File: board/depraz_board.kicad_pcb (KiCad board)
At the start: 2 copper layers, 60 x 40 mm, 15 parts, among them J1 Switches, J2 PIC Programmer, J3 USB, U1 PIC16F1454-IP, U2 TXB0104D, U3 TXB0104D, U4 S-817B20AY-B2-U, U5 PMW3389DM

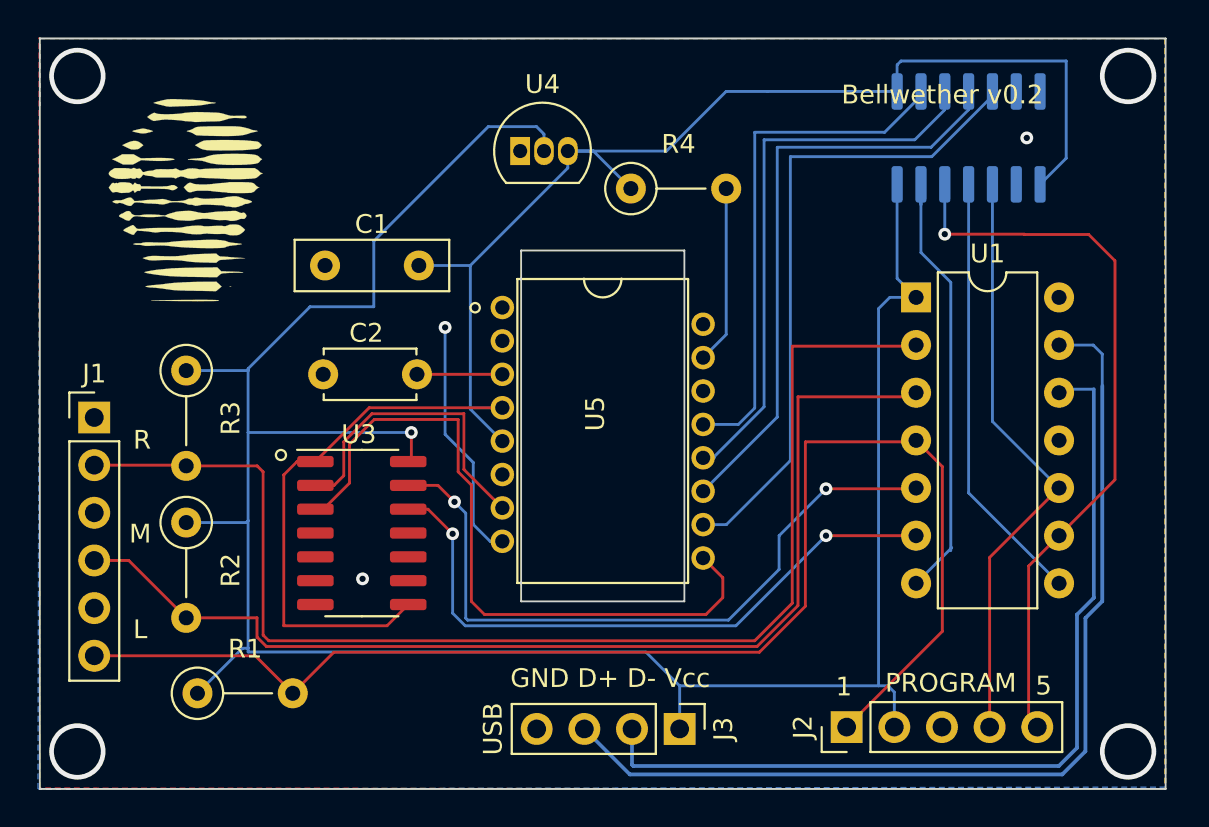
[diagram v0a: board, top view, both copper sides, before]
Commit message: New layout for a STM32 based Depraz replica with quadrature outputs.
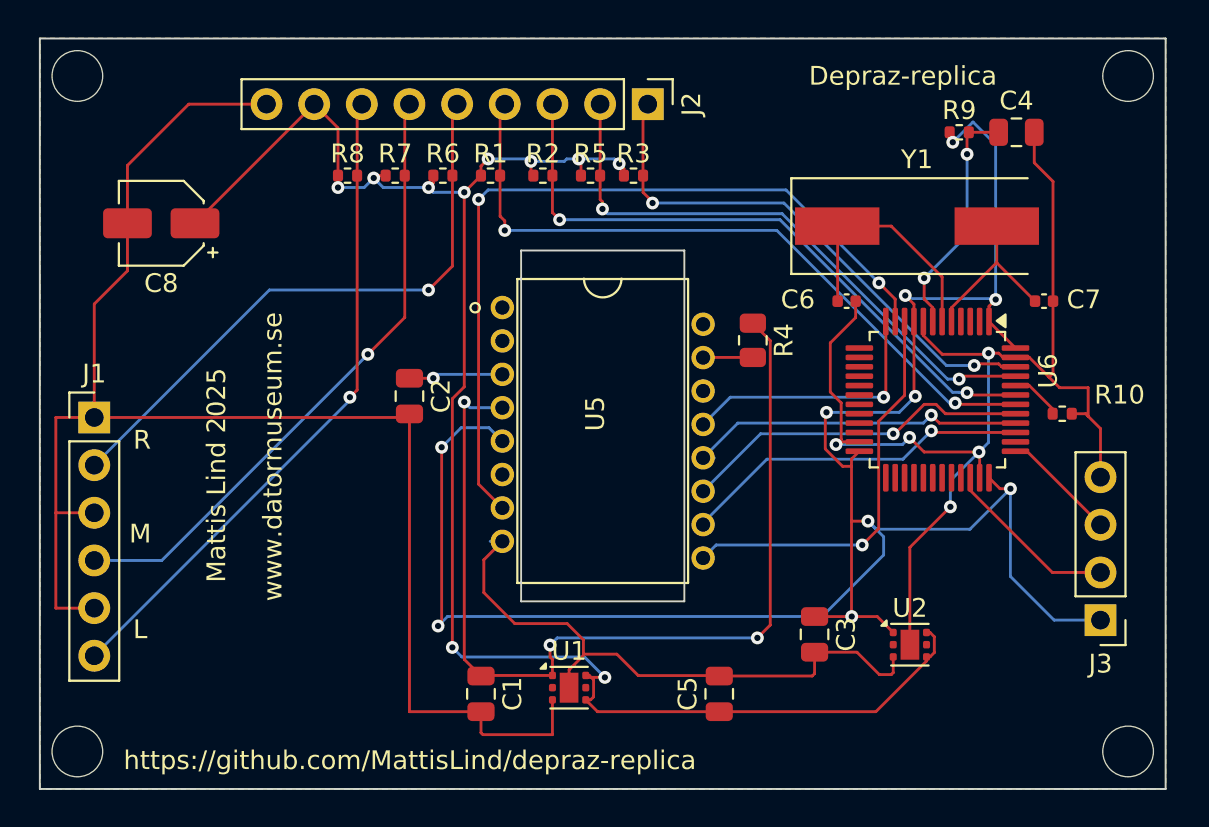
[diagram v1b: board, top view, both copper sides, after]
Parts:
- removed G***: LOGO, depraz_board:pjw
- removed U3: TXB0104D, Package_SO:SOIC-14_3.9x8.7mm_P1.27mm
- removed U4: S-817B20AY-B2-U, Package_TO_SOT_THT:TO-92L_Inline
- added C3: 1u, Capacitor_SMD:C_0805_2012Metric, F.Cu at (161.3, 91.8)
- added C4: 1u, Capacitor_SMD:C_0805_2012Metric, F.Cu at (172.1, 65.0)
- added C5: 1u, Capacitor_SMD:C_0805_2012Metric, F.Cu at (156.2, 94.9)
- added C6: 20p, Capacitor_SMD:C_0402_1005Metric, F.Cu at (163.0, 74.0)
- added C7: 20p, Capacitor_SMD:C_0402_1005Metric, F.Cu at (173.5, 74.0)
- added C8: 22u, Capacitor_SMD:CP_Elec_4x5.4, F.Cu at (126.5, 69.8)
- added H1: MountingHole, MountingHole:MountingHole_2.7mm_M2.5, F.Cu at (122.0, 98.0)
- added H2: MountingHole, MountingHole:MountingHole_2.7mm_M2.5, F.Cu at (122.0, 62.0)
- added H3: MountingHole, MountingHole:MountingHole_2.7mm_M2.5, F.Cu at (178.0, 62.0)
- added H4: MountingHole, MountingHole:MountingHole_2.7mm_M2.5, F.Cu at (178.0, 98.0)
- added R10: 2k, Resistor_SMD:R_0402_1005Metric, F.Cu at (174.5, 80.0)
- added R5: 2k, Resistor_SMD:R_0402_1005Metric, F.Cu at (149.3, 67.3)
- added R6: 2k, Resistor_SMD:R_0402_1005Metric, F.Cu at (141.5, 67.3)
- added R7: 2k, Resistor_SMD:R_0402_1005Metric, F.Cu at (138.9, 67.3)
- added R8: 2k, Resistor_SMD:R_0402_1005Metric, F.Cu at (136.4, 67.3)
- added R9: 2k, Resistor_SMD:R_0402_1005Metric, F.Cu at (169.0, 65.0)
- added U6: STM32F103C8Tx, Package_QFP:LQFP-48_7x7mm_P0.5mm, F.Cu at (167.8, 79.2)
- added Y1: Crystal, Crystal:Crystal_SMD_HC49-SD, F.Cu at (166.8, 70.0)
- C1: value 0.1uF -> 1u; footprint Capacitor_THT:C_Disc_D8.0mm_W2.5mm_P5.00mm -> Capacitor_SMD:C_0805_2012Metric
- C2: footprint Capacitor_THT:C_Disc_D4.7mm_W2.5mm_P5.00mm -> Capacitor_SMD:C_0805_2012Metric
- J2: value PIC Programmer -> Host; footprint Connector_PinHeader_2.54mm:PinHeader_1x05_P2.54mm_Vertical -> Connector_PinHeader_2.54mm:PinHeader_1x09_P2.54mm_Vertical
- J3: value USB -> SWD
- R1, R2, R3: value 1M -> 2k; footprint Resistor_THT:R_Axial_DIN0207_L6.3mm_D2.5mm_P5.08mm_Vertical -> Resistor_SMD:R_0402_1005Metric
- R4: footprint Resistor_THT:R_Axial_DIN0207_L6.3mm_D2.5mm_P5.08mm_Vertical -> Resistor_SMD:R_0805_2012Metric
- U1: value PIC16F1454-IP -> TLV75519PDRV; footprint Package_DIP:DIP-14_W7.62mm -> Package_SON:WSON-6-1EP_2x2mm_P0.65mm_EP1x1.6mm
- U2: value TXB0104D -> TLV75533PDRV; footprint Package_SO:SOIC-14_3.9x8.7mm_P1.27mm -> Package_SON:WSON-6-1EP_2x2mm_P0.65mm_EP1x1.6mm; moved to F.Cu
- moved J2 34.9 mm to (152.4, 63.5), turned to -90 degrees
- moved R1 31.7 mm to (144.0, 67.3)
- moved U1 27.8 mm to (148.2, 94.6)
- moved U2 27.2 mm to (166.4, 92.3), turned to 0 degrees
- moved R2 26.5 mm to (146.8, 67.3), turned to 0 degrees
- moved R3 26.0 mm to (151.6, 67.3), turned to 0 degrees
- moved J3 23.2 mm to (176.5, 91.0), turned to 180 degrees
- moved C1 23.1 mm to (143.5, 94.9), turned to -90 degrees
- moved R4 10.4 mm to (158.0, 76.1), turned to -90 degrees
- moved C2 1.23 mm to (139.7, 79.1), turned to -90 degrees
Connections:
- C1 pad 1: 2V -> 1.9V
- J1 pad 2: Net-(J1-Pad2) -> Net-(J1-Pin_2)
- J1 pad 4: Net-(J1-Pad4) -> Net-(J1-Pin_4)
- J1 pad 6: Net-(J1-Pad6) -> Net-(J1-Pin_6)
- J2 pad 1: Net-(J1-Pad6) -> Net-(J2-Pin_1)
- J2 pad 2: USB_5V -> Net-(J2-Pin_2)
- J2 pad 3: GND -> Net-(J2-Pin_3)
- J2 pad 4: Net-(J2-Pad4) -> Net-(J2-Pin_4)
- J2 pad 5: Net-(J2-Pad5) -> Net-(J1-Pin_2)
- J3 pad 1: USB_5V -> +3.3V
- J3 pad 2: USB_D- -> Net-(J3-Pin_2)
- J3 pad 3: USB_D+ -> Net-(J3-Pin_3)
- R1 pad 1: USB_5V -> +5V
- R1 pad 2: Net-(J1-Pad6) -> Net-(J2-Pin_4)
- R2 pad 1: USB_5V -> +5V
- R2 pad 2: Net-(J1-Pad4) -> Net-(J2-Pin_3)
- R3 pad 1: USB_5V -> +5V
- R3 pad 2: Net-(J1-Pad2) -> Net-(J2-Pin_1)
- R4 pad 1: 2V -> 1.9V
- U1 pad 1: USB_5V -> 1.9V
- U1 pad 2: Net-(J1-Pad2) -> unconnected-(U1-NC-Pad2)
- U1 pad 3: Net-(J1-Pad4) -> GND
- U1 pad 4: Net-(J1-Pad6) -> +5V
- U1 pad 5: Net-(U1-Pad5) -> unconnected-(U1-NC-Pad5)
- U1 pad 6: Net-(U1-Pad6) -> +5V
- U1 pad 7: Net-(U1-Pad7) -> GND
- U2 pad 1: 2V -> +3.3V
- U2 pad 2: Net-(U2-Pad2) -> unconnected-(U2-NC-Pad2)
- U2 pad 3: Net-(U2-Pad3) -> GND
- U2 pad 4: Net-(U2-Pad4) -> +5V
- U2 pad 5: Net-(U2-Pad5) -> unconnected-(U2-NC-Pad5)
- U2 pad 6: Net-(U2-Pad6) -> +5V
- U5 pad 1: Net-(U5-Pad1) -> unconnected-(U5-NC-Pad1)
- U5 pad 10: Net-(U2-Pad5) -> Net-(U5-SCLK)
- U5 pad 11: Net-(U2-Pad4) -> Net-(U5-MOSI)
- U5 pad 12: Net-(U2-Pad3) -> Net-(U5-MISO)
- U5 pad 13: Net-(U2-Pad2) -> Net-(U5-NCS)
- U5 pad 14: Net-(U5-Pad14) -> unconnected-(U5-NC-Pad14)
- U5 pad 16: Net-(U5-Pad16) -> unconnected-(U5-NC-Pad16)
- U5 pad 2: Net-(U5-Pad2) -> unconnected-(U5-NC-Pad2)
- U5 pad 4: 2V -> 1.9V
- U5 pad 5: 2V -> +3.3V
- U5 pad 6: Net-(U5-Pad6) -> unconnected-(U5-GPO-Pad6)
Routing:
- net GND: track 13.0 -> 182.1 mm, vias 3 -> 5
- net USB_5V: track 128.8 -> 0.00 mm, vias 1 -> 0
- net +3.3V: track 0.00 -> 110.7 mm, vias 0 -> 10
- net +5V: track 0.00 -> 92.5 mm, vias 0 -> 10
- net 2V: track 91.8 -> 0.00 mm
- net Net-(J1-Pad6): track 73.3 -> 0.00 mm
- net Net-(J1-Pad2): track 67.3 -> 0.00 mm
- net Net-(J1-Pad4): track 58.4 -> 0.00 mm
- net USB_D+: track 52.3 -> 0.00 mm
- net 1.9V: track 0.00 -> 51.3 mm, vias 0 -> 3
- net USB_D-: track 47.5 -> 0.00 mm
- net Net-(J2-Pad5): track 40.1 -> 0.00 mm, vias 1 -> 0
- net Net-(J2-Pin_4): track 0.00 -> 38.0 mm, vias 0 -> 2
- net Net-(U1-Pad5): track 37.3 -> 0.00 mm, vias 2 -> 0
- net Net-(J1-Pin_6): track 0.00 -> 35.3 mm, vias 0 -> 1
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- added copper zone on B.Cu, net +3.3V
- removed copper zone on B.Cu, net GND
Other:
- net class Default removed
- board text added: "Depraz-replica"
- board text added: "Mattis Lind 2025"
- board text added: "https://github.com/MattisLind/depraz-replica"
- board text added: "www.datormuseum.se"
- board text removed: "1"
- board text removed: "5"
- board text removed: "Bellwether v0.2"
- board text removed: "GND D+ D- Vcc"
- board text removed: "PROGRAM"
- board text removed: "USB"

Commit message: Fixes after review.
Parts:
- Y1: value Crystal -> 8MHz

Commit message: Fixed PCB
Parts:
- added C10: 100n, Capacitor_SMD:C_0402_1005Metric, F.Cu at (171.7, 65.0)
- added C11: 100n, Capacitor_SMD:C_0402_1005Metric, F.Cu at (141.7, 79.7)
- added C12: 100n, Capacitor_SMD:C_0402_1005Metric, F.Cu at (162.9, 83.2)
- added C14: 1u, Capacitor_SMD:C_0805_2012Metric, F.Cu at (146.5, 94.8)
- added C15: 100n, Capacitor_SMD:C_0201_0603Metric, F.Cu at (158.0, 73.5)
- added C9: 100n, Capacitor_SMD:C_0402_1005Metric, F.Cu at (172.8, 75.1)
- added D1: 1.9V PWR, LED_SMD:LED_0603_1608Metric, F.Cu at (154.8, 93.9)
- added D2: 3.3V PWR, LED_SMD:LED_0805_2012Metric, F.Cu at (140.6, 94.3)
- added D3: LED, LED_SMD:LED_0805_2012Metric, F.Cu at (175.3, 73.4)
- added J4: SERIAL, Connector_PinHeader_2.54mm:PinHeader_1x04_P2.54mm_Vertical, F.Cu at (163.1, 89.3)
- added R11: 47, Resistor_SMD:R_0603_1608Metric, F.Cu at (154.5, 97.2)
- added R13: 510, Resistor_SMD:R_0402_1005Metric, F.Cu at (172.2, 73.7)
- added R14: 510, Resistor_SMD:R_0402_1005Metric, F.Cu at (138.9, 97.1)
- C1, C3: value 1u -> 4.7u; footprint Capacitor_SMD:C_0805_2012Metric -> Capacitor_SMD:C_1206_3216Metric
- C2: value 4.7uF -> 4.7u; footprint Capacitor_SMD:C_0805_2012Metric -> Capacitor_SMD:C_1206_3216Metric
- C4: value 1u -> 100n; footprint Capacitor_SMD:C_0805_2012Metric -> Capacitor_SMD:C_0402_1005Metric
- moved C4 34.5 mm to (141.7, 81.5), turned to 180 degrees
- moved U2 32.5 mm to (133.9, 94.0), turned to 180 degrees
- moved C5 25.0 mm to (131.2, 94.1)
- moved C3 24.6 mm to (136.8, 94.1), turned to 90 degrees
- moved C1 8.25 mm to (151.8, 94.7), turned to 90 degrees
- moved C6 6.14 mm to (158.3, 70.0), turned to 180 degrees
- moved C7 4.11 mm to (174.5, 70.0)
- moved C2 1.52 mm to (140.7, 77.9), turned to 180 degrees
- moved U1 1.01 mm to (149.2, 94.8), turned to 180 degrees
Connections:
- net 1.9V renamed +1.9V
- C4 pad 1: Net-(U6-NRST) -> +3.3V
- U1 pad 4: +5V -> +3.3V
- U1 pad 6: +5V -> +3.3V
- U6 pad 12: Net-(U5-NCS) -> unconnected-(U6-PA2-Pad12)
- U6 pad 2: unconnected-(U6-PC13-Pad2) -> Net-(U6-PC13)
- U6 pad 30: unconnected-(U6-PA9-Pad30) -> Net-(J4-Pin_2)
- U6 pad 31: unconnected-(U6-PA10-Pad31) -> Net-(J4-Pin_3)
- U6 pad 38: unconnected-(U6-PA15-Pad38) -> Net-(U5-NCS)
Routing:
- net GND: track 182.1 -> 34.9 mm, vias 5 -> 0
- net +3.3V: track 110.7 -> 22.1 mm, vias 10 -> 11
- net +5V: track 92.5 -> 65.0 mm, vias 10 -> 8
- net +1.9V: track 51.3 -> 61.7 mm
- net Net-(J4-Pin_2): track 0.00 -> 6.73 mm
- net Net-(J4-Pin_3): track 0.00 -> 5.95 mm
- net Net-(U5-NCS): track 14.3 -> 18.9 mm
- net Net-(D1-A): track 0.00 -> 3.41 mm
- net Net-(U6-PC13): track 0.00 -> 2.61 mm
- net Net-(U5-Vddpix): track 5.04 -> 2.49 mm, vias 1 -> 0
- net Net-(D2-A): track 0.00 -> 2.35 mm
- net Net-(D3-A): track 0.00 -> 1.79 mm
- net Net-(U5-SCLK): track 18.8 -> 19.6 mm
- net Net-(J3-Pin_2): track 9.43 -> 10.1 mm, vias 0 -> 1
- net Net-(U5-NRESET): track 43.0 -> 42.4 mm, vias 2 -> 1
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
